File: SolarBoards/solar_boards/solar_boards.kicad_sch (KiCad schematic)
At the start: 14 parts, among them U8 SPV1040T

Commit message: Changes to solar boards
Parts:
- added H1, H2, H3, H4: MountingHole_Pad, inspireFly:MountingHole_2mm_custom, symbol Mechanical:MountingHole_Pad
- added J1: M55-6001242R, inspireFly:HARWIN_M55-6001242R, symbol inspireFly:M55-6001242R
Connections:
- net GND: now also H1.1, H2.1, H3.1, H4.1

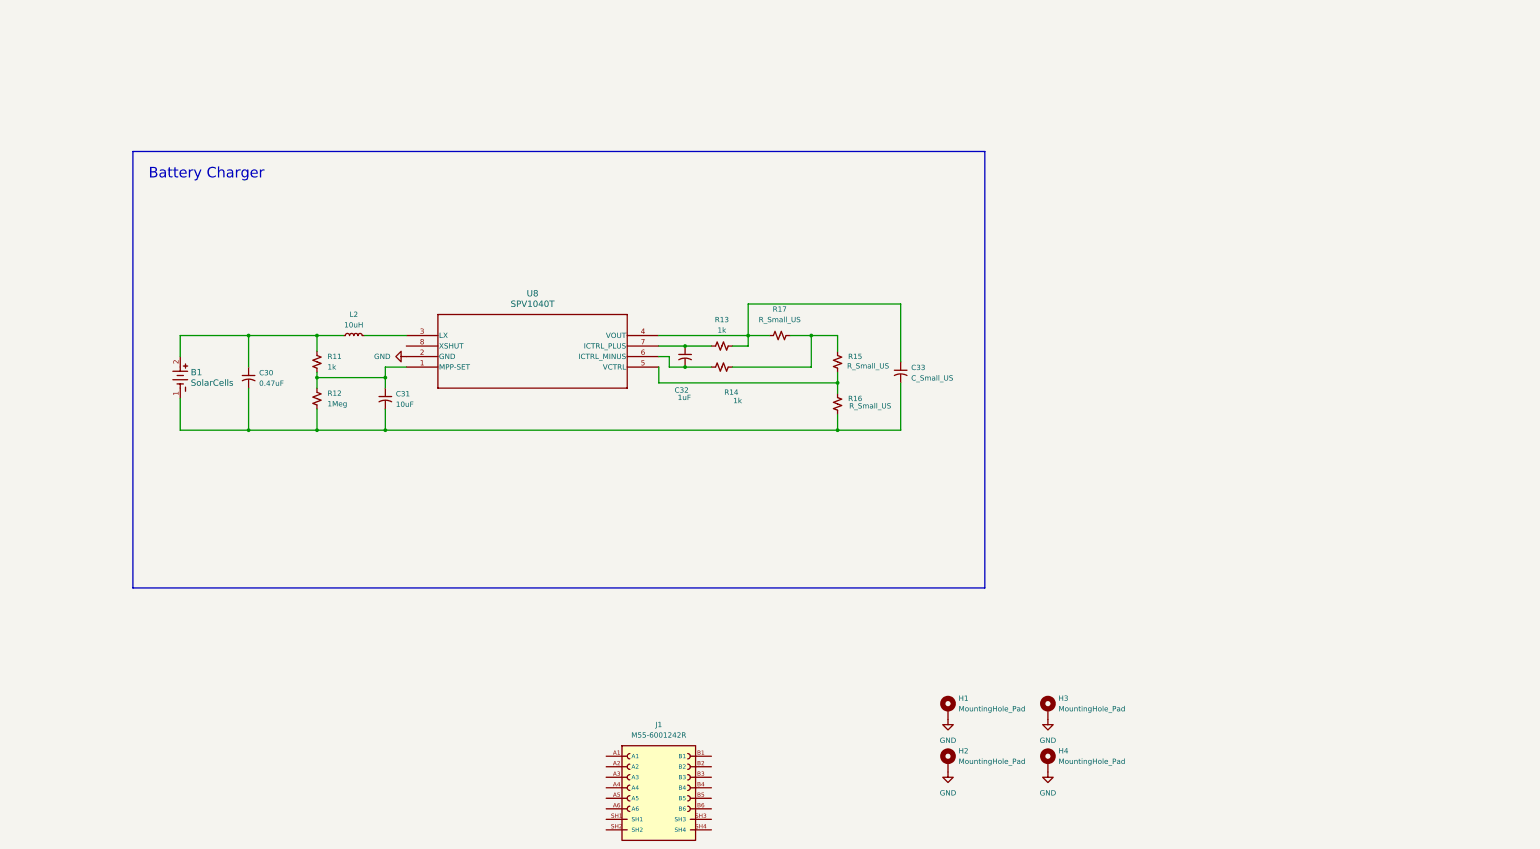
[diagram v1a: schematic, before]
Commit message: started battery harvester
imported harvester and started wiring up
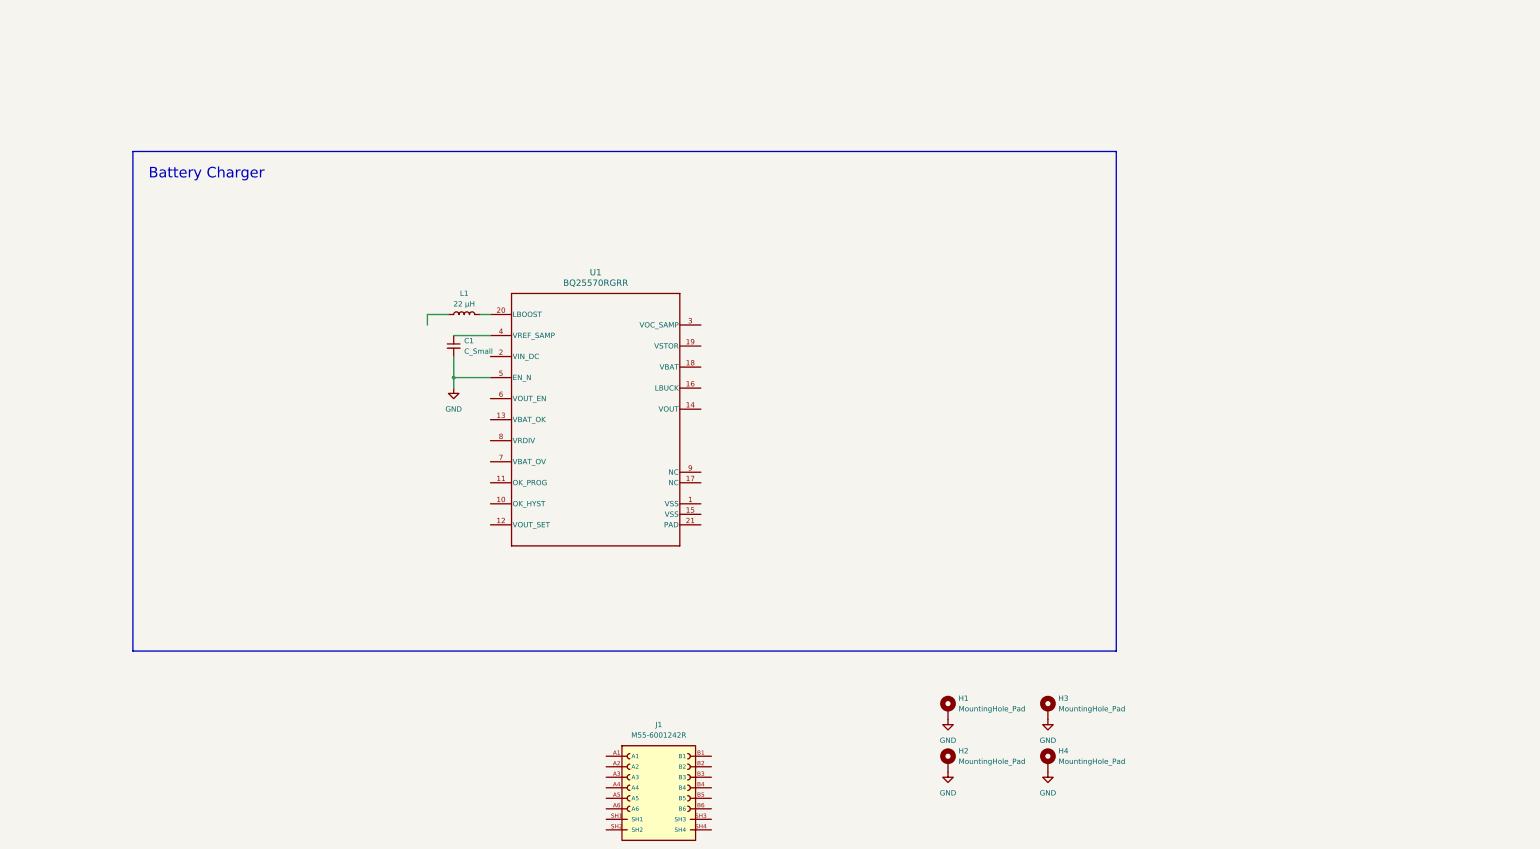
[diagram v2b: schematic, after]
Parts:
- removed B1: SolarCells, KXOB25-05X3F_IXY, symbol inspirefly:SolarCells
- removed C30: 0.47uF, symbol Device:C_Small_US
- removed C31: 10uF, symbol Device:C_Small_US
- removed C32: 1uF, symbol Device:C_Small_US
- removed C33: C_Small_US, symbol Device:C_Small_US
- removed L2: 10uH, symbol Device:L_Small
- removed R11, R13, R14: 1k, symbol Device:R_Small_US
- removed R12: 1Meg, symbol Device:R_Small_US
- removed R15, R16, R17: R_Small_US, symbol Device:R_Small_US
- removed U8: SPV1040T, SOIC_1040T_STM, symbol inspirefly:SPV1040T
- added C1: C_Small, symbol Device:C_Small
- added L1: 22 µH, symbol Device:L
- added U1: BQ25570RGRR, footprints:RGR0020A_NV, symbol batteryharvester:BQ25570RGRR
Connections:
- net GND: now also C1.2, U1.5 (EN_N)
- new net: L1.2, U1.20 (LBOOST)
- new net: C1.1, U1.4 (VREF_SAMP)

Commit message: began wiring
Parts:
- added C2: C_Small, symbol Device:C_Small
- added L2: L, symbol Device:L
- added R1, R2, R3, R4, R5, R6, R7, R8: R_US, symbol Device:R_US
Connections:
- net GND: now also U1.1 (VSS), C2.2, R3.1, R6.1, R8.1
- net at U1.10 (OK_HYST): now also R4.1, R5.2
- net at U1.11 (OK_PROG): now also R5.1, R6.2
- net at U1.12 (VOUT_SET): now also R7.1, R8.2
- net at U1.14 (VOUT): now also C2.1, L2.2
- net at U1.16 (LBUCK): now also L2.1
- net at U1.7 (VBAT_OV): now also R2.1, R3.2
- net at U1.8 (VRDIV): now also R2.2, R4.2, R7.2
- no-connect marks 0 -> 1
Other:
- moved on the sheet: C1

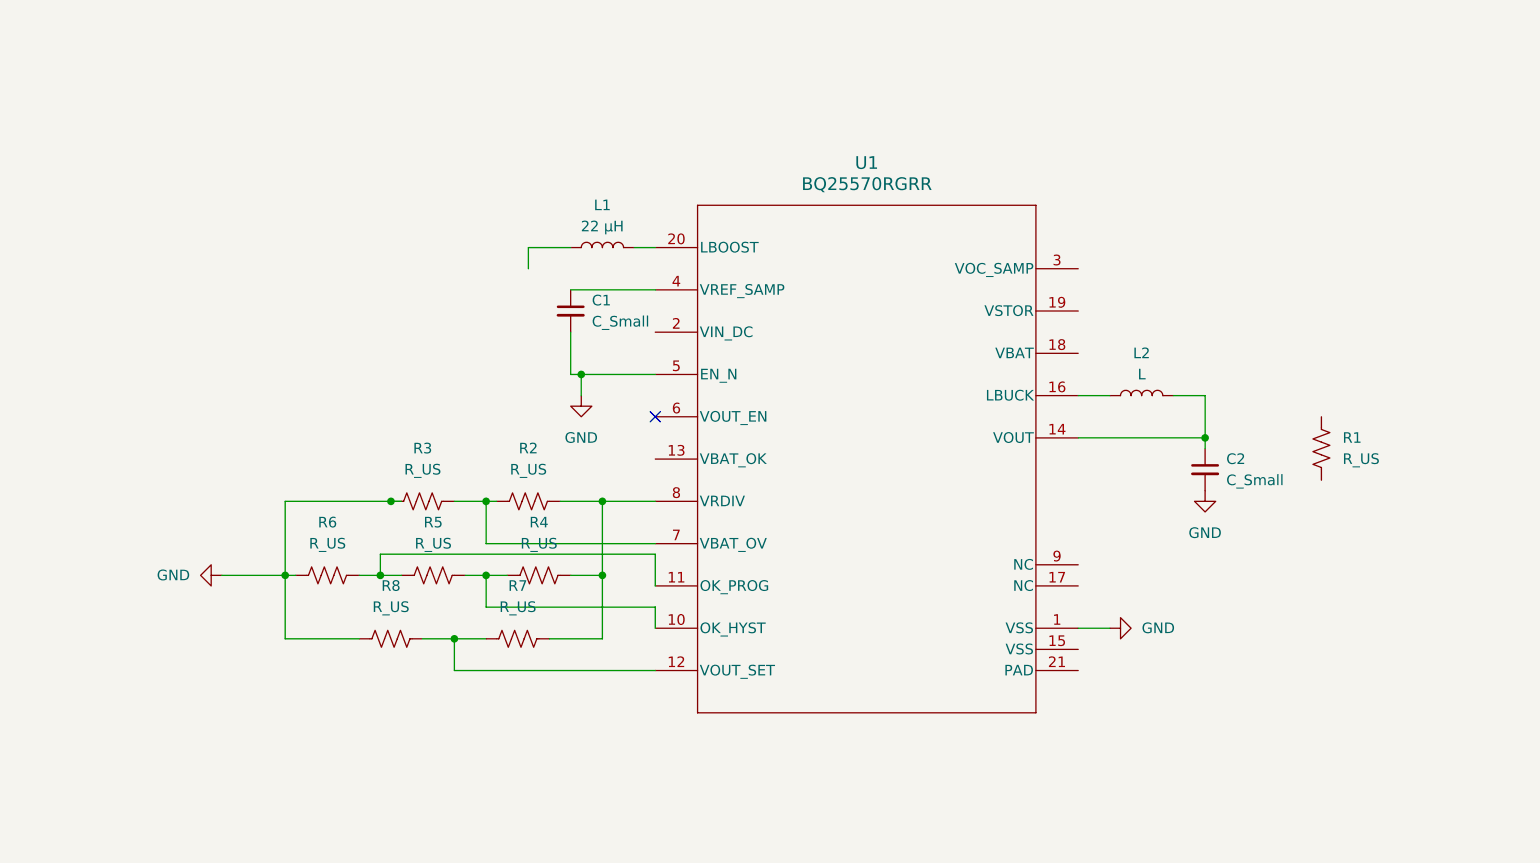
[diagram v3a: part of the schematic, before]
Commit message: added new boost converter and added elements
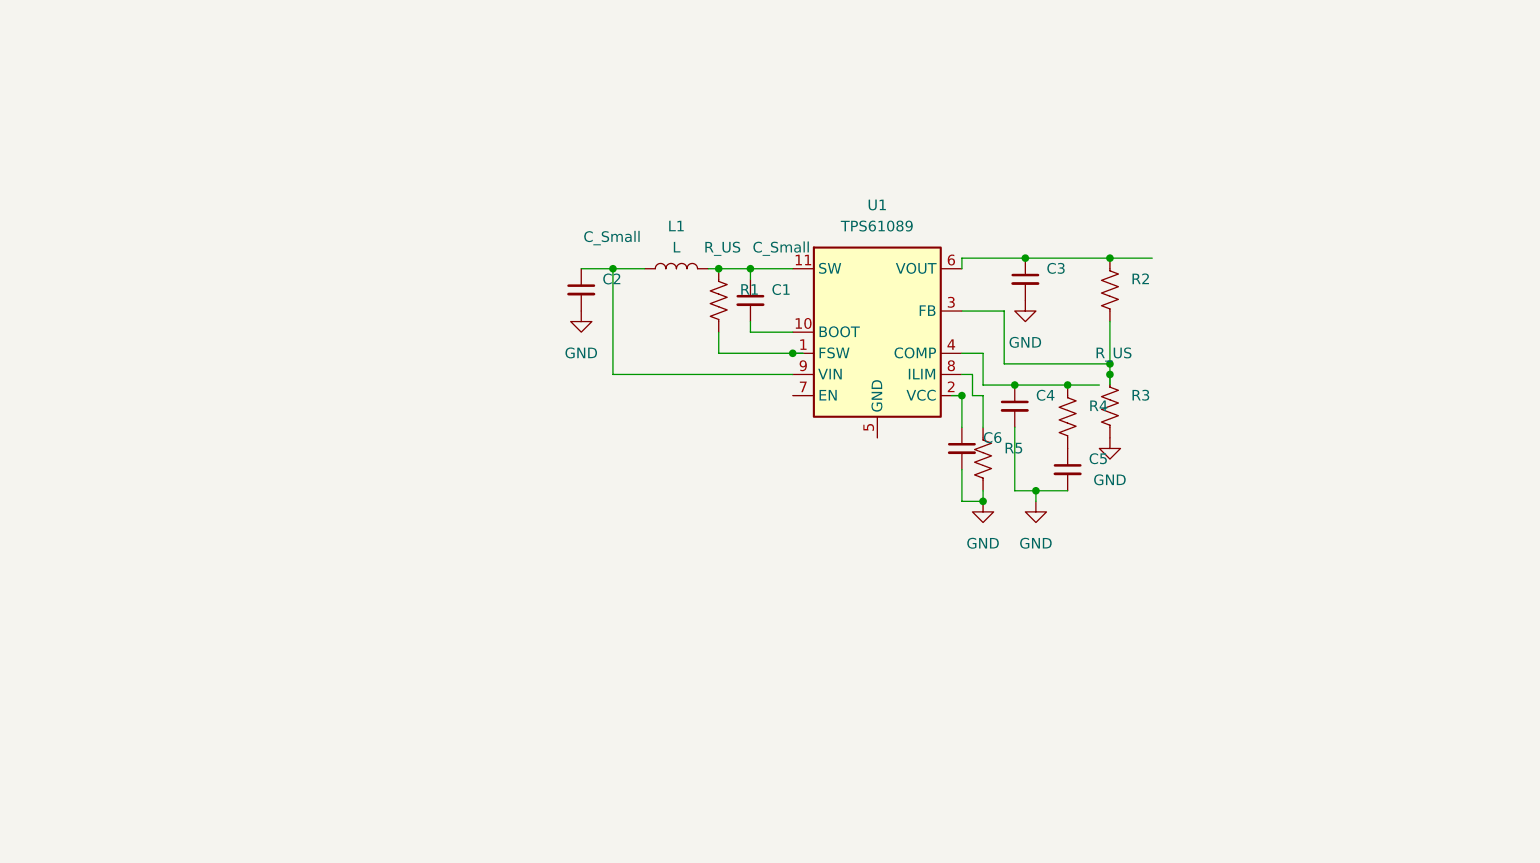
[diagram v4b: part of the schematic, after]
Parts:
- removed L2: L, symbol Device:L
- removed R6, R7, R8: R_US, symbol Device:R_US
- removed U1: BQ25570RGRR, footprints:RGR0020A_NV, symbol batteryharvester:BQ25570RGRR
- added C3, C4, C5, C6: C_Small, symbol Device:C_Small
- added U1: TPS61089, Package_DFN_QFN:Texas_VQFN-RNR0011A-11, symbol Regulator_Switching:TPS61089
- L1: value 22 µH -> L
- R2: value R_US -> ~
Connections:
- net GND: now also R3.2, R5.2, C3.2, C4.2, C5.2, C6.2; no longer C1.2, R3.1
- net at R4.1: now also C4.1, U1.4 (COMP); no longer R5.2
- net at R5.1: now also U1.8 (ILIM)
- net at C2.1: now also L1.1, U1.9 (VIN)
- net at L1.2: now also C1.1, R1.1, U1.11 (SW)
- net at R2.1: now also C3.1, U1.6 (VOUT); no longer R3.2
- net at R4.2: now also C5.1; no longer R2.2
- net at R1.2: now also U1.1 (FSW)
- new net: R2.2, R3.1, U1.3 (FB)
- new net: C1.2, U1.10 (BOOT)
- new net: C6.1, U1.2 (VCC)
- no-connect marks 1 -> 0

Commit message: boost converter values, will add solar cell
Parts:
- C1: renamed from C2; value C_Small -> 22uF
- C3: value C_Small -> 47 uF
- C3: renamed from C6; value C_Small -> 0.1uF
- C4: renamed from C1; value C_Small -> 0.1uF
- C5: value C_Small -> 2.2 uF
- C6: renamed from C4; value C_Small -> 0.1uF
- L1: value L -> 10µH
- R1: renamed from R2; value ~ -> 560k
- R2: renamed from R3; value R_US -> 100k
- RFreq: renamed from R1; value R_US -> 301k
- RILIM: renamed from R5; value R_US -> 257k
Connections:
- net at C6.1, R4.1, U1.4 (COMP): now also R1.2, R2.1, U1.3 (FB)
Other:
- moved on the sheet: C1, C3, C5, C6, L1, R1, R2, R4, RFreq, RILIM

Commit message: Solar Board Schematic and Routing
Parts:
- removed C1: 22uF, symbol Device:C_Small
- removed C3: 47 uF, symbol Device:C_Small
- removed C3, C4, C6: 0.1uF, symbol Device:C_Small
- removed C5: 2.2 uF, symbol Device:C_Small
- removed RFreq: 301k, symbol Device:R_US
- removed RILIM: 257k, symbol Device:R_US
- removed U1: TPS61089, Package_DFN_QFN:Texas_VQFN-RNR0011A-11, symbol Regulator_Switching:TPS61089
- added C1, C2, C3, C6: 10uF, Capacitor_SMD:C_0402_1005Metric_Pad0.74x0.62mm_HandSolder, symbol Device:C
- added C4, C8, C9: 1uF, Capacitor_SMD:C_0402_1005Metric_Pad0.74x0.62mm_HandSolder, symbol Device:C
- added C5: 4.7uF, Capacitor_SMD:C_0402_1005Metric_Pad0.74x0.62mm_HandSolder, symbol Device:C
- added C7: 100nF, Capacitor_SMD:C_0402_1005Metric_Pad0.74x0.62mm_HandSolder, symbol Device:C
- added D1, D2, D3, D4, D5, D6: CDBQC0130L, inspireFly:DIODFN100X60X55-2N, symbol Device:D_Schottky
- added R3, R5, R6: 200K, Resistor_SMD:R_0402_1005Metric_Pad0.72x0.64mm_HandSolder, symbol Device:R_US
- added R7: 820K, Resistor_SMD:R_0402_1005Metric_Pad0.72x0.64mm_HandSolder, symbol Device:R_US
- added SC1, SC2, SC3, SC4, SC5, SC6: Solar_Cell, inspireFly:SOLAR_KXOB25-14X1F-TR, symbol Device:Solar_Cell
- added U1: LTC3105EDD-TRPBF, inspireFly:DFN-10_DD_LIT, symbol inspireFly:LTC3105EDD-TRPBF
- added U2: OPT3004DNPR, inspireFly:DNP0006A, symbol 2026-04-11_18-01-49:OPT3004DNPR
- added U3: LM73100RPWR, inspireFly:IC_LM73100RPWR, symbol inspireFly:LM73100RPWR
- L1: value 10µH -> 10uH; footprint (none) -> inspireFly:WE-LQFS_3818
- R1: value 560k -> 332K; footprint (none) -> Resistor_SMD:R_0402_1005Metric_Pad0.72x0.64mm_HandSolder
- R2: value 100k -> 820K; footprint (none) -> Resistor_SMD:R_0402_1005Metric_Pad0.72x0.64mm_HandSolder
- R4: value R_US -> 549K; footprint (none) -> Resistor_SMD:R_0402_1005Metric_Pad0.72x0.64mm_HandSolder
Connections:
- net GND: now also J1.A1, J1.A2, J1.A3, J1.A4, J1.A5, J1.A6, J1.SH1, J1.SH2, J1.SH3, J1.SH4, R1.2, C1.2, C2.2, C3.2, C4.1, C5.2, C6.2, C7.2, C8.2, C9.2, D6.2 (A), R3.1, R5.2, R6.1, SC6.2 (-), U1.11 (EPAD), U1.3 (FBLDO), U2.2 (ADDR), U2.3 (GND), U2.7 (PAD), U3.4 (PGTH), U3.8 (GND), U3.9 (IMON); no longer R2.2
- net at R4.2: now also R5.1, U3.1 (EN/UVLO)
- net at L1.1: now also U1.7 (SW)
- net at L1.2: now also R2.2, R4.1, C3.1, C6.1, C8.1, R7.2, U1.9 (VOUT), U3.5 (IN)
- net at R1.1: now also U1.5 (MPPC)
- net EXTERNAL_VOLTAGE: now reaches J1.B1
- net EXTERNAL_VOLTAGE: now also J1.B2, J1.B3, J1.B4, C9.1, U3.6 (OUT)
- net I2C_SCL: now reaches J1.B5
- net I2C_SCL: now also U2.4 (SCL)
- net I2C_SDA: now reaches J1.B6
- net I2C_SDA: now also U2.6 (SDA)
- new net: C1.1, C2.1, D1.1 (K), SC1.1 (+), U1.6 (VIN)
- new net: D1.2 (A), D2.1 (K), SC1.2 (-), SC2.1 (+)
- new net: D2.2 (A), D3.1 (K), SC2.2 (-), SC3.1 (+)
- new net: D4.2 (A), D5.1 (K), SC4.2 (-), SC5.1 (+)
- new net: D5.2 (A), D6.1 (K), SC5.2 (-), SC6.1 (+)
- new net: D3.2 (A), D4.1 (K), SC3.2 (-), SC4.1 (+)
- new net: R2.1, R3.2, U1.1 (FB)
- new net: C4.2, U1.10 (AUX)
- new net: R6.2, R7.1, U3.2 (OVLO)
- new net +2.2V: C5.1, C7.1, U1.2 (LDO), U2.1 (VDD)
- no-connect marks 0 -> 5
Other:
- note added: "74406032100"
- note added: "Assuming slightly colder than Room temp (25C) - .8 x 4.14V = 3.31V"
- note added: "DC DC with MPPT"
- note added: "OVLO - apx 6.12V"
- note added: "R_MPPC = 3.31V / 10uA = 331K round up to 332k"
- note added: "Set to about 5.1V, .1V to account for connector and series loss"
- note added: "ULVO - apx 4.5V"
- note added: "V_MPPC ≈ 0.76-0.80 × Voc"
- note removed: "Battery Charger"
- moved on the sheet: H1, H2, H3, H4, J1
